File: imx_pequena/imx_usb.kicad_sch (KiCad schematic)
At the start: 15 parts, among them J3 USB_B_Micro, J4 USB_C_Receptacle

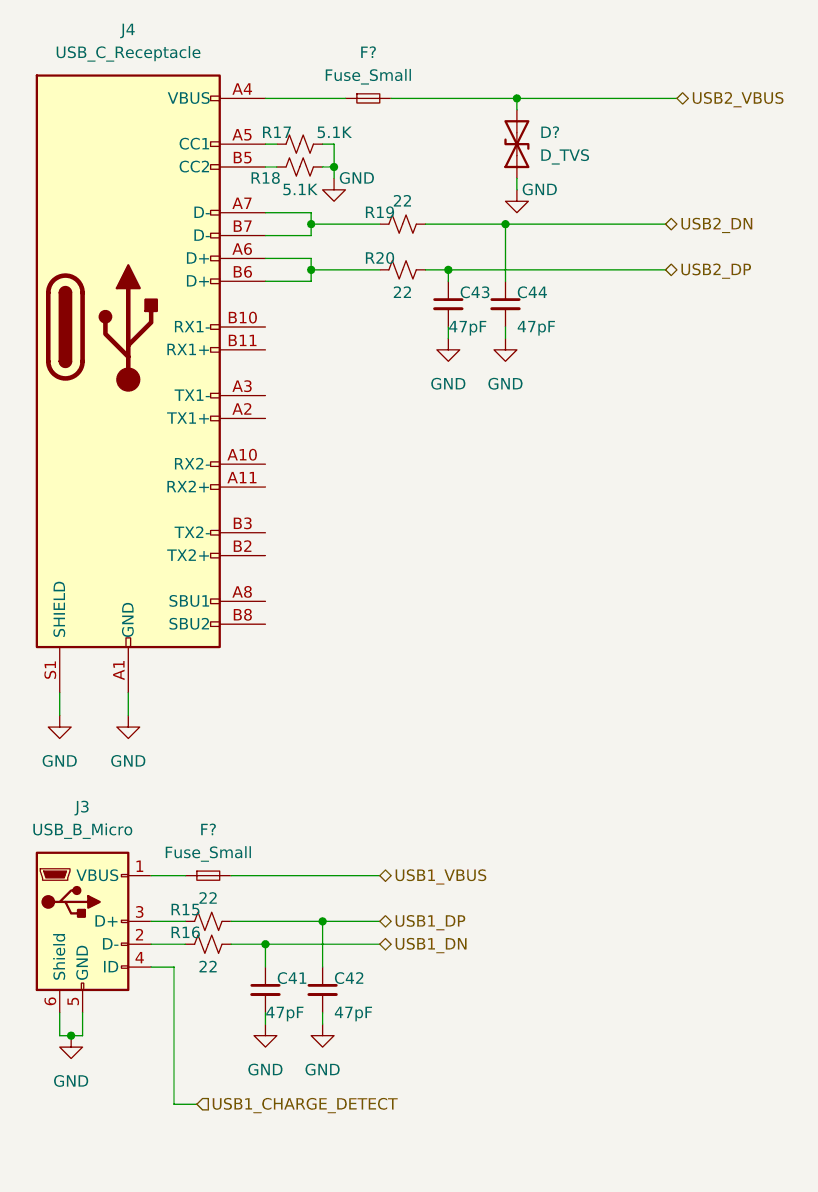
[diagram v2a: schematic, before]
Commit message: Pinout updates
Updated pinout files, changed pinout of gpio 1 and 3
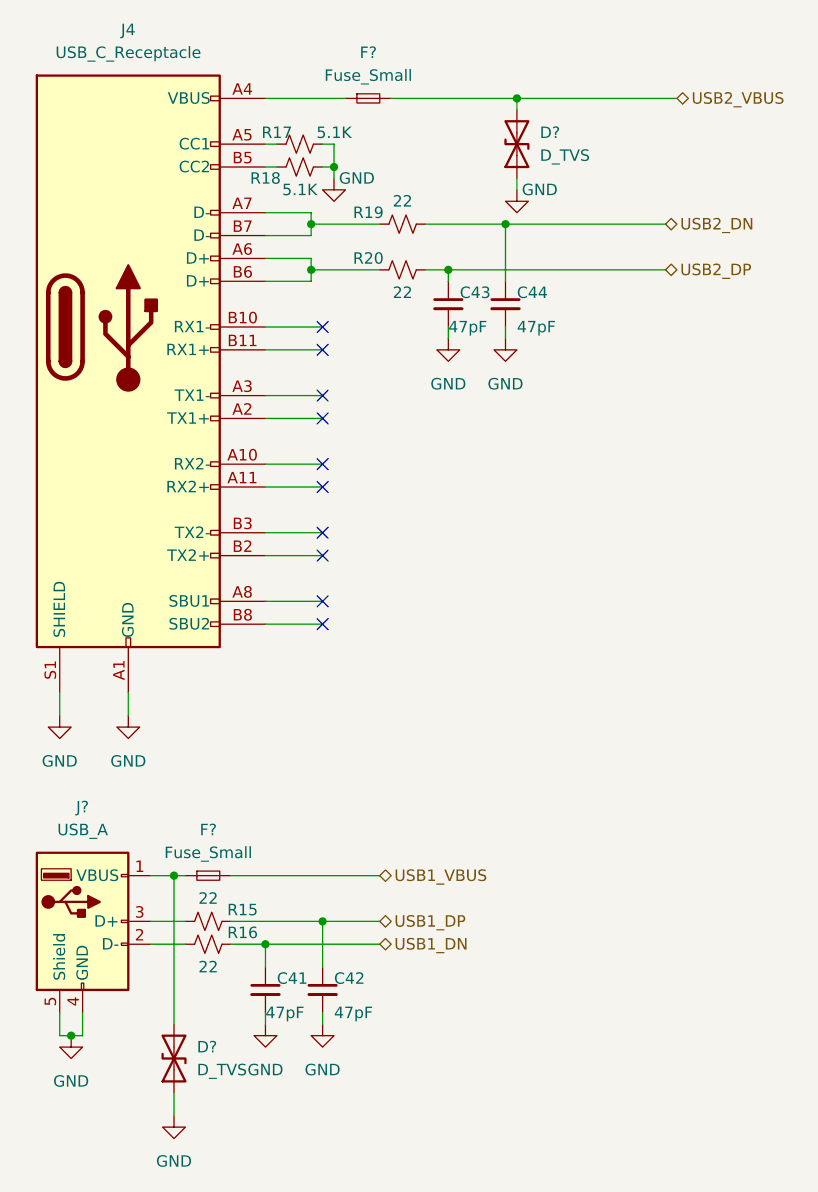
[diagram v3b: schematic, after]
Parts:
- removed J3: USB_B_Micro, symbol Connector:USB_B_Micro
- added D?: D_TVS, symbol Device:D_TVS
- added J?: USB_A, symbol Connector:USB_A
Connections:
- net GND: now also D?.1 (A1), J?.4 (GND), J?.5 (Shield)
- net at F?.1: now also D?.2 (A2), J?.1 (VBUS)
- net at R16.1: now also J?.2 (D-)
- net at R15.1: now also J?.3 (D+)
- no-connect marks 0 -> 10
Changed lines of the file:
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@@
   (junction (at 71.12 39.37) (diameter 0) (color 0 0 0 0)
   )
+  (junction (at 34.29 111.76) (diameter 0) (color 0 0 0 0)
+  )
   (junction (at 44.45 119.38) (diameter 0) (color 0 0 0 0)
   )
@@
   (junction (at 72.39 25.4) (diameter 0) (color 0 0 0 0)
   )
+  (no_connect (at 50.8 73.66))
+  (no_connect (at 50.8 60.96))
+  (no_connect (at 50.8 81.28))
+  (no_connect (at 50.8 58.42))
+  (no_connect (at 50.8 68.58))
+  (no_connect (at 50.8 50.8))
+  (no_connect (at 50.8 66.04))
+  (no_connect (at 50.8 83.82))
+  (no_connect (at 50.8 76.2))
+  (no_connect (at 50.8 53.34))
   (wire (pts (xy 62.23 44.45) (xy 64.77 44.45))
     (stroke (width 0) (type default) (color 0 0 0 0))
   )
+  (wire (pts (xy 44.45 53.34) (xy 50.8 53.34))
+    (stroke (width 0) (type default) (color 0 0 0 0))
+  )
   (wire (pts (xy 40.64 116.84) (xy 50.8 116.84))
     (stroke (width 0) (type default) (color 0 0 0 0))
@@
     (stroke (width 0) (type default) (color 0 0 0 0))
   )
+  (wire (pts (xy 34.29 111.76) (xy 35.56 111.76))
+    (stroke (width 0) (type default) (color 0 0 0 0))
+  )
   (wire (pts (xy 72.39 25.4) (xy 90.17 25.4))
     (stroke (width 0) (type default) (color 0 0 0 0))
@@
     (stroke (width 0) (type default) (color 0 0 0 0))
   )
-  (wire (pts (xy 34.29 137.16) (xy 36.83 137.16))
-    (stroke (width 0) (type default) (color 0 0 0 0))
-  )
-  (wire (pts (xy 34.29 121.92) (xy 34.29 137.16))
-    (stroke (width 0) (type default) (color 0 0 0 0))
-  )
   (wire (pts (xy 40.64 111.76) (xy 57.15 111.76))
     (stroke (width 0) (type default) (color 0 0 0 0))
@@
     (stroke (width 0) (type default) (color 0 0 0 0))
   )
+  (wire (pts (xy 44.45 76.2) (xy 50.8 76.2))
+    (stroke (width 0) (type default) (color 0 0 0 0))
+  )
   (wire (pts (xy 52.07 30.48) (xy 52.07 33.02))
     (stroke (width 0) (type default) (color 0 0 0 0))
@@
     (stroke (width 0) (type default) (color 0 0 0 0))
   )
-  (wire (pts (xy 31.75 121.92) (xy 34.29 121.92))
-    (stroke (width 0) (type default) (color 0 0 0 0))
-  )
   (wire (pts (xy 49.53 39.37) (xy 49.53 38.1))
     (stroke (width 0) (type default) (color 0 0 0 0))
@@
     (stroke (width 0) (type default) (color 0 0 0 0))
   )
+  (wire (pts (xy 34.29 111.76) (xy 34.29 128.27))
+    (stroke (width 0) (type default) (color 0 0 0 0))
+  )
   (wire (pts (xy 50.8 127) (xy 50.8 128.27))
     (stroke (width 0) (type default) (color 0 0 0 0))
@@
     (stroke (width 0) (type default) (color 0 0 0 0))
   )
-  (wire (pts (xy 31.75 111.76) (xy 35.56 111.76))
+  (wire (pts (xy 44.45 81.28) (xy 50.8 81.28))
+    (stroke (width 0) (type default) (color 0 0 0 0))
+  )
+  (wire (pts (xy 31.75 111.76) (xy 34.29 111.76))
+    (stroke (width 0) (type default) (color 0 0 0 0))
+  )
+  (wire (pts (xy 44.45 50.8) (xy 50.8 50.8))
     (stroke (width 0) (type default) (color 0 0 0 0))
   )
@@
     (stroke (width 0) (type default) (color 0 0 0 0))
   )
+  (wire (pts (xy 34.29 135.89) (xy 34.29 138.43))
+    (stroke (width 0) (type default) (color 0 0 0 0))
+  )
+  (wire (pts (xy 44.45 66.04) (xy 50.8 66.04))
+    (stroke (width 0) (type default) (color 0 0 0 0))
+  )
+  (wire (pts (xy 44.45 60.96) (xy 50.8 60.96))
+    (stroke (width 0) (type default) (color 0 0 0 0))
+  )
   (wire (pts (xy 64.77 44.45) (xy 64.77 45.72))
     (stroke (width 0) (type default) (color 0 0 0 0))
   )
+  (wire (pts (xy 44.45 83.82) (xy 50.8 83.82))
+    (stroke (width 0) (type default) (color 0 0 0 0))
+  )
+  (wire (pts (xy 44.45 58.42) (xy 50.8 58.42))
+    (stroke (width 0) (type default) (color 0 0 0 0))
+  )
   (wire (pts (xy 44.45 45.72) (xy 49.53 45.72))
     (stroke (width 0) (type default) (color 0 0 0 0))
@@
     (stroke (width 0) (type default) (color 0 0 0 0))
   )
+  (wire (pts (xy 44.45 68.58) (xy 50.8 68.58))
+    (stroke (width 0) (type default) (color 0 0 0 0))
+  )
   (wire (pts (xy 40.64 119.38) (xy 44.45 119.38))
     (stroke (width 0) (type default) (color 0 0 0 0))
@@
   )
   (wire (pts (xy 49.53 45.72) (xy 49.53 44.45))
+    (stroke (width 0) (type default) (color 0 0 0 0))
+  )
+  (wire (pts (xy 44.45 73.66) (xy 50.8 73.66))
     (stroke (width 0) (type default) (color 0 0 0 0))
   )
@@
     (effects (font (size 1.27 1.27)) (justify left))
   )
-  (hierarchical_label "USB1_CHARGE_DETECT" (shape input) (at 36.83 137.16 0)
-    (effects (font (size 1.27 1.27)) (justify left))
-  )
   (symbol (lib_id "power:GND") (at 44.45 128.27 0) (unit 1)
     (in_bom yes) (on_board yes) (fields_autoplaced)
@@
     )
     (property "Datasheet" "" (id 3) (at 72.39 35.56 0)
+      (effects (font (size 1.27 1.27)) hide)
+    )
+    (pin "1")
+  )
+  (symbol (lib_id "power:GND") (at 34.29 138.43 0) (unit 1)
+    (in_bom yes) (on_board yes) (fields_autoplaced)
+    (property "Reference" "#PWR?" (id 0) (at 34.29 144.78 0)
+      (effects (font (size 1.27 1.27)) hide)
+    )
+    (property "Value" "GND" (id 1) (at 34.29 143.51 0))
+    (property "Footprint" "" (id 2) (at 34.29 138.43 0)
+      (effects (font (size 1.27 1.27)) hide)
+    )
+    (property "Datasheet" "" (id 3) (at 34.29 138.43 0)
       (effects (font (size 1.27 1.27)) hide)
     )
@@
     (pin "2")
   )
+  (symbol (lib_id "Device:D_TVS") (at 34.29 132.08 90) (unit 1)
+    (in_bom yes) (on_board yes) (fields_autoplaced)
+    (property "Reference" "D?" (id 0) (at 36.83 130.8099 90)
+      (effects (font (size 1.27 1.27)) (justify right))
+    )
+    (property "Value" "D_TVS" (id 1) (at 36.83 133.3499 90)
+      (effects (font (size 1.27 1.27)) (justify right))
+    )
+    (property "Footprint" "" (id 2) (at 34.29 132.08 0)
+      (effects (font (size 1.27 1.27)) hide)
+    )
+    (property "Datasheet" "~" (id 3) (at 34.29 132.08 0)
+      (effects (font (size 1.27 1.27)) hide)
+    )
+    (pin "1")
+    (pin "2")
+  )
   (symbol (lib_id "power:GND") (at 64.77 52.07 0) (unit 1)
     (in_bom yes) (on_board yes) (fields_autoplaced)
@@
   (symbol (lib_id "Device:R_Small_US") (at 38.1 119.38 90) (unit 1)
     (in_bom yes) (on_board yes)
-    (property "Reference" "R16" (id 0) (at 35.56 118.11 90))
+    (property "Reference" "R16" (id 0) (at 41.91 118.11 90))
     (property "Value" "22" (id 1) (at 38.1 121.92 90))
     (property "Footprint" "" (id 2) (at 38.1 119.38 0)
@@
   (symbol (lib_id "Device:R_Small_US") (at 59.69 39.37 90) (unit 1)
     (in_bom yes) (on_board yes)
-    (property "Reference" "R19" (id 0) (at 57.15 38.1 90))
+    (property "Reference" "R19" (id 0) (at 55.88 38.1 90))
     (property "Value" "22" (id 1) (at 59.69 36.83 90))
     (property "Footprint" "" (id 2) (at 59.69 39.37 0)
@@
     (pin "1")
     (pin "2")
+  )
+  (symbol (lib_id "Connector:USB_A") (at 24.13 116.84 0) (unit 1)
+    (in_bom yes) (on_board yes) (fields_autoplaced)
+    (property "Reference" "J?" (id 0) (at 24.13 104.14 0))
+    (property "Value" "USB_A" (id 1) (at 24.13 106.68 0))
+    (property "Footprint" "" (id 2) (at 27.94 118.11 0)
+      (effects (font (size 1.27 1.27)) hide)
+    )
+    (property "Datasheet" " ~" (id 3) (at 27.94 118.11 0)
+      (effects (font (size 1.27 1.27)) hide)
+    )
+    (pin "1")
+    (pin "2")
+    (pin "3")
+    (pin "4")
+    (pin "5")
   )
   (symbol (lib_id "power:GND") (at 52.07 34.29 0) (unit 1)
@@
   (symbol (lib_id "Device:R_Small_US") (at 59.69 44.45 90) (unit 1)
     (in_bom yes) (on_board yes)
-    (property "Reference" "R20" (id 0) (at 57.15 43.18 90))
+    (property "Reference" "R20" (id 0) (at 55.88 43.18 90))
     (property "Value" "22" (id 1) (at 59.69 46.99 90))
     (property "Footprint" "" (id 2) (at 59.69 44.45 0)
@@
     (pin "2")
   )
-  (symbol (lib_id "Connector:USB_B_Micro") (at 24.13 116.84 0) (unit 1)
-    (in_bom yes) (on_board yes) (fields_autoplaced)
-    (property "Reference" "J3" (id 0) (at 24.13 104.14 0))
-    (property "Value" "USB_B_Micro" (id 1) (at 24.13 106.68 0))
-    (property "Footprint" "" (id 2) (at 27.94 118.11 0)
-      (effects (font (size 1.27 1.27)) hide)
-    )
-    (property "Datasheet" "~" (id 3) (at 27.94 118.11 0)
-      (effects (font (size 1.27 1.27)) hide)
-    )
-    (pin "1")
-    (pin "2")
-    (pin "3")
-    (pin "4")
-    (pin "5")
-    (pin "6")
-  )
   (symbol (lib_id "Device:D_TVS") (at 72.39 30.48 90) (unit 1)
     (in_bom yes) (on_board yes) (fields_autoplaced)
@@
   (symbol (lib_id "Device:R_Small_US") (at 38.1 116.84 90) (unit 1)
     (in_bom yes) (on_board yes)
-    (property "Reference" "R15" (id 0) (at 35.56 115.57 90))
+    (property "Reference" "R15" (id 0) (at 41.91 115.57 90))
     (property "Value" "22" (id 1) (at 38.1 114.3 90))
     (property "Footprint" "" (id 2) (at 38.1 116.84 0)

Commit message: Part Assignment
Assigned GPIOs and assigned footprints to most parts
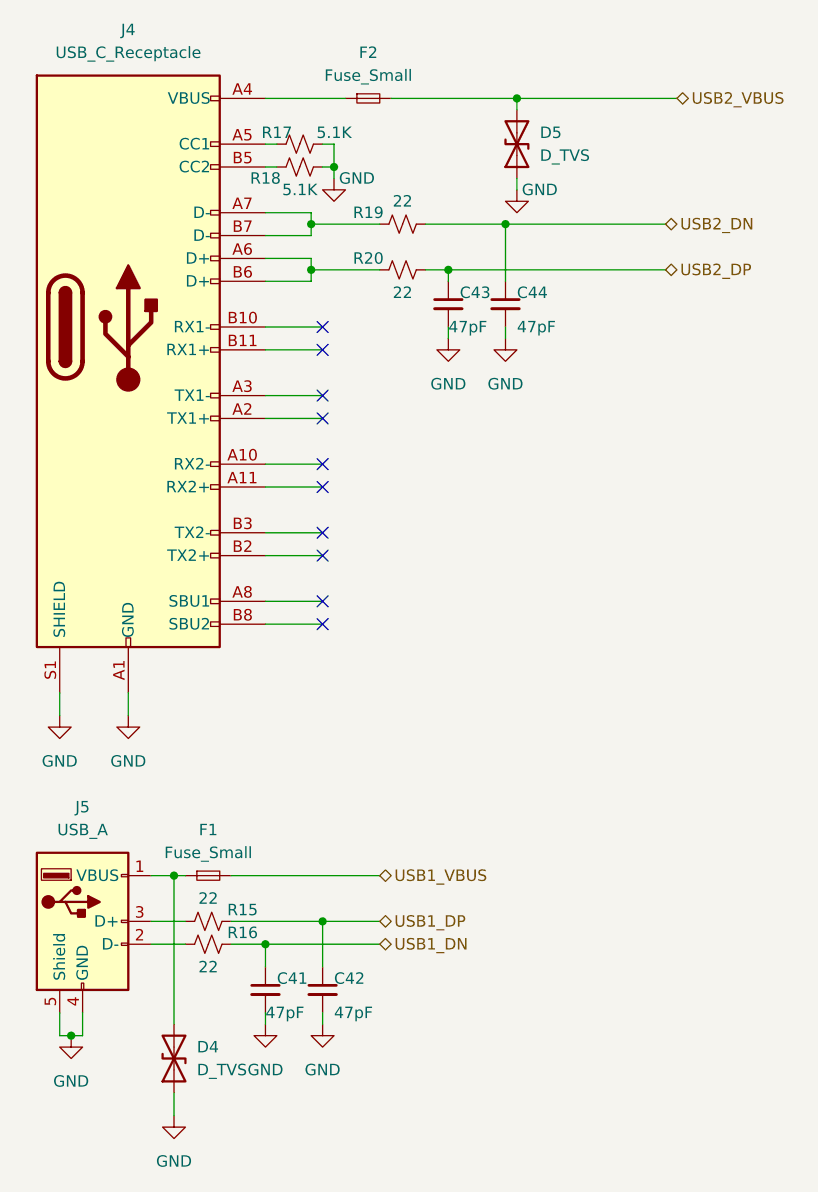
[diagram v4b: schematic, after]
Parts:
- C41, C42, C43, C44: footprint (none) -> Capacitor_SMD:C_0402_1005Metric
- D4, D5: renamed from D?; footprint (none) -> Diode_SMD:D_SOD-123
- F1, F2: renamed from F?; footprint (none) -> Resistor_SMD:R_1206_3216Metric
- J4: footprint (none) -> Connector_USB:USB_C_Receptacle_Amphenol_12401610E4-2A_CircularHoles
- J5: renamed from J?; footprint (none) -> Connector_USB:USB_A_Molex_67643_Horizontal
- R15, R16, R17, R18, R19, R20: footprint (none) -> Resistor_SMD:R_0402_1005Metric
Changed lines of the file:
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@@
   (symbol (lib_id "power:GND") (at 72.39 35.56 0) (unit 1)
     (in_bom yes) (on_board yes)
-    (property "Reference" "#PWR?" (id 0) (at 72.39 41.91 0)
+    (property "Reference" "#PWR0165" (id 0) (at 72.39 41.91 0)
       (effects (font (size 1.27 1.27)) hide)
     )
@@
   (symbol (lib_id "power:GND") (at 34.29 138.43 0) (unit 1)
     (in_bom yes) (on_board yes) (fields_autoplaced)
-    (property "Reference" "#PWR?" (id 0) (at 34.29 144.78 0)
+    (property "Reference" "#PWR0164" (id 0) (at 34.29 144.78 0)
       (effects (font (size 1.27 1.27)) hide)
     )
@@
   (symbol (lib_id "Device:Fuse_Small") (at 38.1 111.76 0) (unit 1)
     (in_bom yes) (on_board yes) (fields_autoplaced)
-    (property "Reference" "F?" (id 0) (at 38.1 106.68 0))
+    (property "Reference" "F1" (id 0) (at 38.1 106.68 0))
     (property "Value" "Fuse_Small" (id 1) (at 38.1 109.22 0))
-    (property "Footprint" "" (id 2) (at 38.1 111.76 0)
+    (property "Footprint" "Resistor_SMD:R_1206_3216Metric" (id 2) (at 38.1 111.76 0)
       (effects (font (size 1.27 1.27)) hide)
     )
@@
   (symbol (lib_id "Device:D_TVS") (at 34.29 132.08 90) (unit 1)
     (in_bom yes) (on_board yes) (fields_autoplaced)
-    (property "Reference" "D?" (id 0) (at 36.83 130.8099 90)
+    (property "Reference" "D4" (id 0) (at 36.83 130.8099 90)
       (effects (font (size 1.27 1.27)) (justify right))
     )
@@
       (effects (font (size 1.27 1.27)) (justify right))
     )
-    (property "Footprint" "" (id 2) (at 34.29 132.08 0)
+    (property "Footprint" "Diode_SMD:D_SOD-123" (id 2) (at 34.29 132.08 0)
       (effects (font (size 1.27 1.27)) hide)
     )
@@
     (property "Reference" "R16" (id 0) (at 41.91 118.11 90))
     (property "Value" "22" (id 1) (at 38.1 121.92 90))
-    (property "Footprint" "" (id 2) (at 38.1 119.38 0)
+    (property "Footprint" "Resistor_SMD:R_0402_1005Metric" (id 2) (at 38.1 119.38 0)
       (effects (font (size 1.27 1.27)) hide)
     )
@@
       (effects (font (size 1.27 1.27)) (justify left))
     )
-    (property "Footprint" "" (id 2) (at 44.45 124.46 0)
+    (property "Footprint" "Capacitor_SMD:C_0402_1005Metric" (id 2) (at 44.45 124.46 0)
       (effects (font (size 1.27 1.27)) hide)
     )
@@
       (effects (font (size 1.27 1.27)) (justify left))
     )
-    (property "Footprint" "" (id 2) (at 50.8 124.46 0)
+    (property "Footprint" "Capacitor_SMD:C_0402_1005Metric" (id 2) (at 50.8 124.46 0)
       (effects (font (size 1.27 1.27)) hide)
     )
@@
       (effects (font (size 1.27 1.27)) (justify left))
     )
-    (property "Footprint" "" (id 2) (at 64.77 48.26 0)
+    (property "Footprint" "Capacitor_SMD:C_0402_1005Metric" (id 2) (at 64.77 48.26 0)
       (effects (font (size 1.27 1.27)) hide)
     )
@@
     (property "Reference" "R18" (id 0) (at 44.45 34.29 90))
     (property "Value" "5.1K" (id 1) (at 48.26 35.56 90))
-    (property "Footprint" "" (id 2) (at 48.26 33.02 0)
+    (property "Footprint" "Resistor_SMD:R_0402_1005Metric" (id 2) (at 48.26 33.02 0)
       (effects (font (size 1.27 1.27)) hide)
     )
@@
   (symbol (lib_id "Device:Fuse_Small") (at 55.88 25.4 0) (unit 1)
     (in_bom yes) (on_board yes) (fields_autoplaced)
-    (property "Reference" "F?" (id 0) (at 55.88 20.32 0))
+    (property "Reference" "F2" (id 0) (at 55.88 20.32 0))
     (property "Value" "Fuse_Small" (id 1) (at 55.88 22.86 0))
-    (property "Footprint" "" (id 2) (at 55.88 25.4 0)
+    (property "Footprint" "Resistor_SMD:R_1206_3216Metric" (id 2) (at 55.88 25.4 0)
       (effects (font (size 1.27 1.27)) hide)
     )
@@
     (property "Reference" "R19" (id 0) (at 55.88 38.1 90))
     (property "Value" "22" (id 1) (at 59.69 36.83 90))
-    (property "Footprint" "" (id 2) (at 59.69 39.37 0)
+    (property "Footprint" "Resistor_SMD:R_0402_1005Metric" (id 2) (at 59.69 39.37 0)
       (effects (font (size 1.27 1.27)) hide)
     )
@@
   (symbol (lib_id "Connector:USB_A") (at 24.13 116.84 0) (unit 1)
     (in_bom yes) (on_board yes) (fields_autoplaced)
-    (property "Reference" "J?" (id 0) (at 24.13 104.14 0))
+    (property "Reference" "J5" (id 0) (at 24.13 104.14 0))
     (property "Value" "USB_A" (id 1) (at 24.13 106.68 0))
-    (property "Footprint" "" (id 2) (at 27.94 118.11 0)
+    (property "Footprint" "Connector_USB:USB_A_Molex_67643_Horizontal" (id 2) (at 27.94 118.11 0)
       (effects (font (size 1.27 1.27)) hide)
     )
@@
     (property "Reference" "R17" (id 0) (at 45.72 29.21 90))
     (property "Value" "5.1K" (id 1) (at 52.07 29.21 90))
-    (property "Footprint" "" (id 2) (at 48.26 30.48 0)
+    (property "Footprint" "Resistor_SMD:R_0402_1005Metric" (id 2) (at 48.26 30.48 0)
       (effects (font (size 1.27 1.27)) hide)
     )
@@
     (property "Reference" "J4" (id 0) (at 29.21 17.78 0))
     (property "Value" "USB_C_Receptacle" (id 1) (at 29.21 20.32 0))
-    (property "Footprint" "" (id 2) (at 33.02 50.8 0)
+    (property "Footprint" "Connector_USB:USB_C_Receptacle_Amphenol_12401610E4-2A_CircularHoles" (id 2) (at 33.02 50.8 0)
       (effects (font (size 1.27 1.27)) hide)
     )
@@
       (effects (font (size 1.27 1.27)) (justify left))
     )
-    (property "Footprint" "" (id 2) (at 71.12 48.26 0)
+    (property "Footprint" "Capacitor_SMD:C_0402_1005Metric" (id 2) (at 71.12 48.26 0)
       (effects (font (size 1.27 1.27)) hide)
     )
@@
     (property "Reference" "R20" (id 0) (at 55.88 43.18 90))
     (property "Value" "22" (id 1) (at 59.69 46.99 90))
-    (property "Footprint" "" (id 2) (at 59.69 44.45 0)
+    (property "Footprint" "Resistor_SMD:R_0402_1005Metric" (id 2) (at 59.69 44.45 0)
       (effects (font (size 1.27 1.27)) hide)
     )
@@
   (symbol (lib_id "Device:D_TVS") (at 72.39 30.48 90) (unit 1)
     (in_bom yes) (on_board yes) (fields_autoplaced)
-    (property "Reference" "D?" (id 0) (at 74.93 29.2099 90)
+    (property "Reference" "D5" (id 0) (at 74.93 29.2099 90)
       (effects (font (size 1.27 1.27)) (justify right))
     )
@@
       (effects (font (size 1.27 1.27)) (justify right))
     )
-    (property "Footprint" "" (id 2) (at 72.39 30.48 0)
+    (property "Footprint" "Diode_SMD:D_SOD-123" (id 2) (at 72.39 30.48 0)
       (effects (font (size 1.27 1.27)) hide)
     )
@@
     (property "Reference" "R15" (id 0) (at 41.91 115.57 90))
     (property "Value" "22" (id 1) (at 38.1 114.3 90))
-    (property "Footprint" "" (id 2) (at 38.1 116.84 0)
-      (effects (font (size 1.27 1.27)) hide)
-    )
+    (property "Footprint" "Resistor_SMD:R_0402_1005Metric" (id 2) (at 38.1 116.84 0)
+      (effects (font (size 1.27 1.27)) hide)
+    )

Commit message: lots of updates
Set design rules, fixed ERC, etc....
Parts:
- J4: footprint Connector_USB:USB_C_Receptacle_Amphenol_12401610E4-2A_CircularHoles -> (none)
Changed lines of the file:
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@@
     (property "Reference" "J4" (id 0) (at 29.21 17.78 0))
     (property "Value" "USB_C_Receptacle" (id 1) (at 29.21 20.32 0))
-    (property "Footprint" "Connector_USB:USB_C_Receptacle_Amphenol_12401610E4-2A_CircularHoles" (id 2) (at 33.02 50.8 0)
+    (property "Footprint" "" (id 2) (at 33.02 50.8 0)
       (effects (font (size 1.27 1.27)) hide)
     )
